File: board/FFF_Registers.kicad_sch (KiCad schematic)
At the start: 20 parts, among them U48 74F573, U49 74F541, U50 74F573, U51 74F541, U52 74F573, U53 74F541, U54 74F573, U55 74F541, U56 74F32, U57 74F02

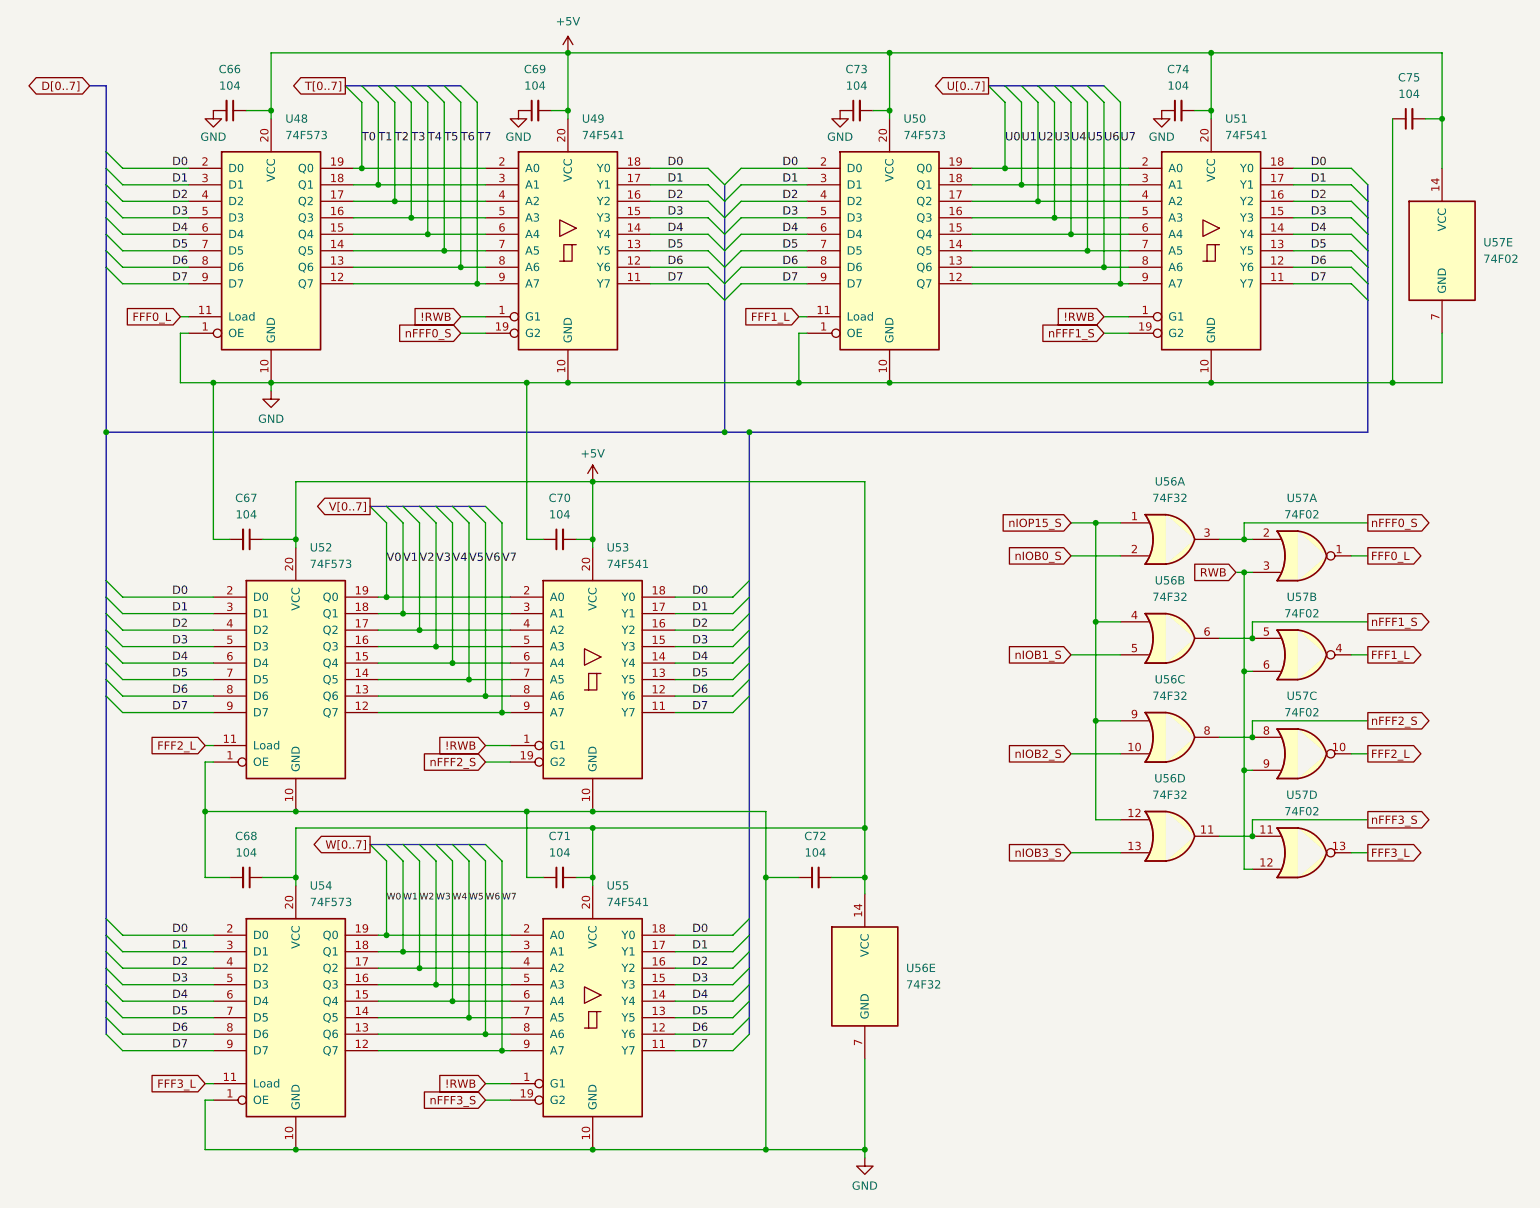
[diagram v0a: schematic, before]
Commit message: V2.0 changes with new S register and simplified logic
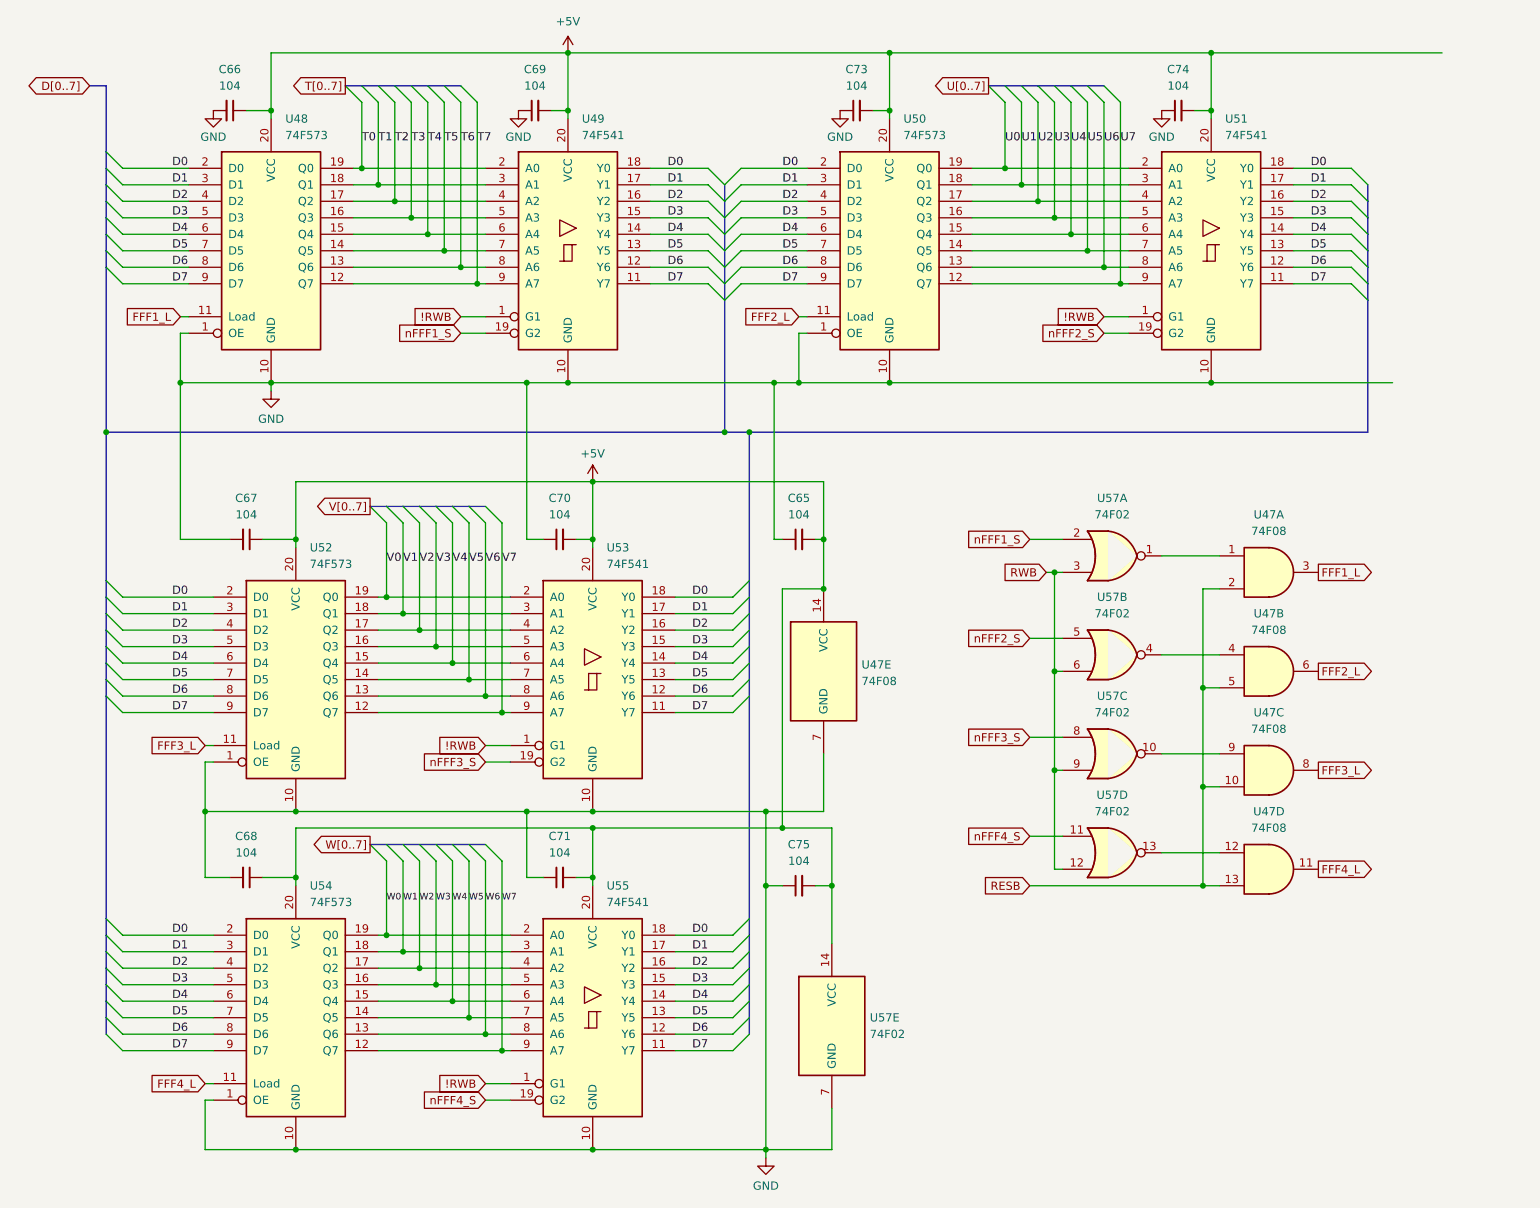
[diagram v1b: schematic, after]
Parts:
- removed C72: 104, Capacitor_THT:C_Disc_D5.0mm_W2.5mm_P5.00mm, symbol Device:C_Small
- removed U56: 74F32, Package_DIP:DIP-14_W7.62mm_Socket_LongPads, symbol 74xx:74LS32
- added C65: 104, Capacitor_THT:C_Disc_D5.0mm_W2.5mm_P5.00mm, symbol Device:C_Small
- added U47: 74F08, Package_DIP:DIP-14_W7.62mm_Socket_LongPads, symbol 74xx:74LS08
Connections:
- net nFFF0_S is gone; now on net nFFF1_S: U49.19 (G2), U57.2
- net +5V: now also C65.2, U47.14 (VCC)
- net FFF1_L: now also U48.11 (Load), U47.3; no longer U50.11 (Load), U57.4
- net FFF2_L: now also U50.11 (Load), U47.6; no longer U52.11 (Load), U57.10
- net FFF3_L: now also U52.11 (Load), U47.8; no longer U54.11 (Load), U57.13
- net GND: now also C65.1, U47.7 (GND)
- net nFFF1_S: no longer U51.19 (G2), U57.5
- net nFFF2_S: now also U51.19 (G2), U57.5; no longer U53.19 (G2), U57.8
- net nFFF3_S: now also U53.19 (G2), U57.8; no longer U55.19 (G2), U57.11
- net FFF0_L: no longer names the net of U57.1
- net FFF0_L: now also U47.1; no longer U48.11 (Load)
- new net: U47.12, U57.13
- new net: U47.4, U57.4
- new net: U47.9, U57.10
- new net FFF4_L: U47.11, U54.11 (Load)
- new net RESB: U47.10, U47.13, U47.2, U47.5
- new net nFFF4_S: U55.19 (G2), U57.11
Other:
- moved on the sheet: C75, U57A, U57B, U57C, U57D

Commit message: V2.0 updates and new hydra breakout and counter cards.
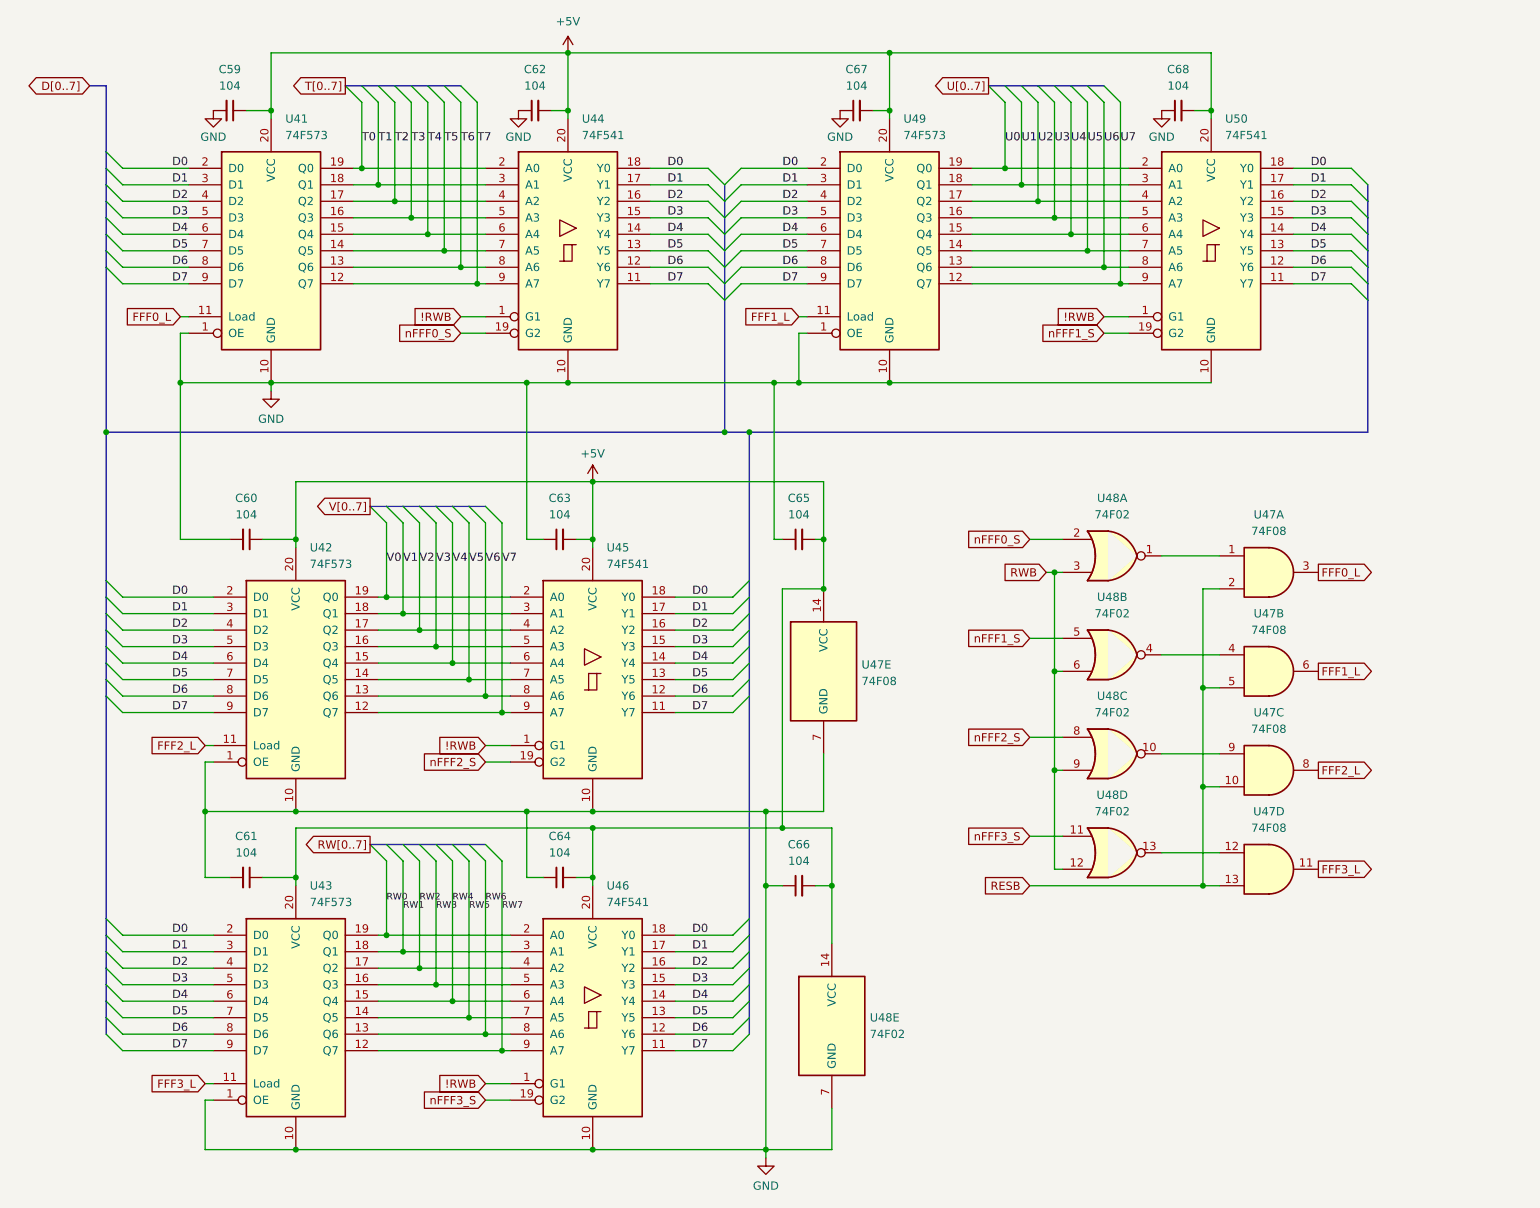
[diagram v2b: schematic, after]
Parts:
- added unit 1 of U47
- added unit 4 of U47
- added unit 3 of U47
- added unit 5 of U47
- renumbered C66 to C59, C67 to C60, C68 to C61, C69 to C62, C70 to C63, C71 to C64, C75 to C66, C73 to C67, C74 to C68, U48 to U41, U52 to U42, U54 to U43, U49 to U44, U53 to U45, U55 to U46, U57 to U48, U50 to U49, U51 to U50
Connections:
- net nFFF4_S is gone; now on net nFFF3_S: U46.19 (G2), U48.11
- net +5V: now also U47.14 (VCC); no longer U47.14 (VCC)
- net FFF1_L: now also U47.6, U49.11 (Load); no longer U41.11 (Load), U47.3
- net FFF2_L: now also U42.11 (Load), U47.8; no longer U47.6, U49.11 (Load)
- net FFF3_L: now also U43.11 (Load), U47.11; no longer U42.11 (Load), U47.8
- net GND: now also U47.7 (GND); no longer U47.7 (GND)
- net RESB: now also U47.10, U47.13, U47.2; no longer U47.10, U47.13, U47.2
- net nFFF1_S: now also U48.5, U50.19 (G2); no longer U44.19 (G2), U48.2
- net nFFF2_S: now also U45.19 (G2), U48.8; no longer U48.5, U50.19 (G2)
- net nFFF3_S: no longer U45.19 (G2), U48.8
- net at U48.1: now also U47.1; no longer U47.1
- net at U48.13: now also U47.12; no longer U47.12
- net at U48.10: now also U47.9; no longer U47.9
- removed net FFF4_L: U43.11 (Load), U47.11
- net W0 renamed RW0
- net W1 renamed RW1
- net W2 renamed RW2
- net W3 renamed RW3
- net W4 renamed RW4
- net W5 renamed RW5
- net W6 renamed RW6
- net W7 renamed RW7
- new net FFF0_L: U41.11 (Load), U47.3
- new net nFFF0_S: U44.19 (G2), U48.2
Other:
- title: FFFx Registers and Logic -> ZeroPage $00/$01 Mirror Memory and RAM/ROM Bank Logic
